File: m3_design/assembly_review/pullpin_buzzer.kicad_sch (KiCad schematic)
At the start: 10 parts, among them J123 BM02B-GHS-TBT(LF)(SN), Q123 AO3400A

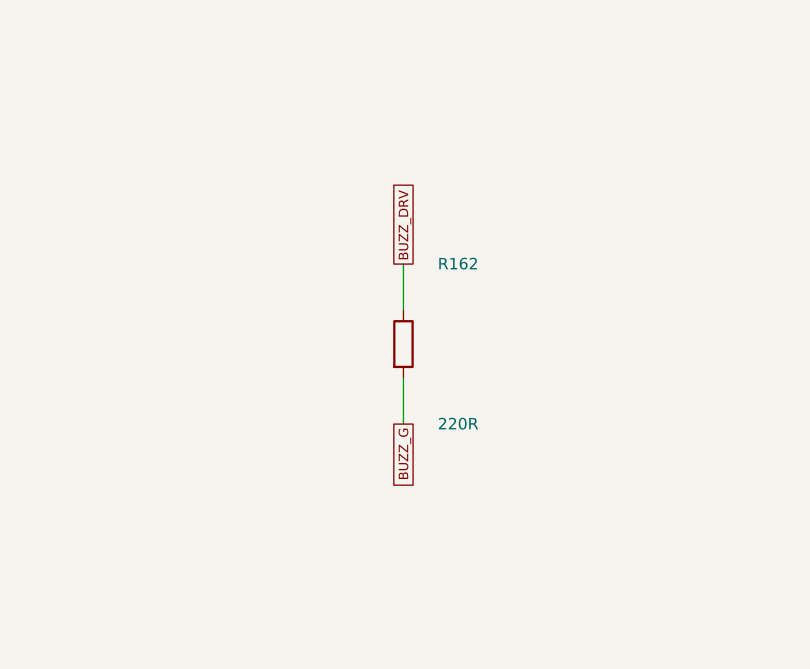
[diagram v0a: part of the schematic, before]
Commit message: R10 review round 3 and fix pass: ten-lens review of 883d2db5 (0 Critical, 7 Major, 49 Minor); In2 GND under the pyro column (S-8), U9 power path widened, In2 re-cut for the port control nets, GND vias at port-signal layer changes, crystal In2 GND restored, stitching, silkscreen >= 0.15 mm; gates: arcs, K-loader, S-8/S-9, wider critical set, needless hops, plate masses; R410 budget, R162 1k, F6 ride-through restated (OQ-5/OQ-6); board 579575bd..., check.sh 0
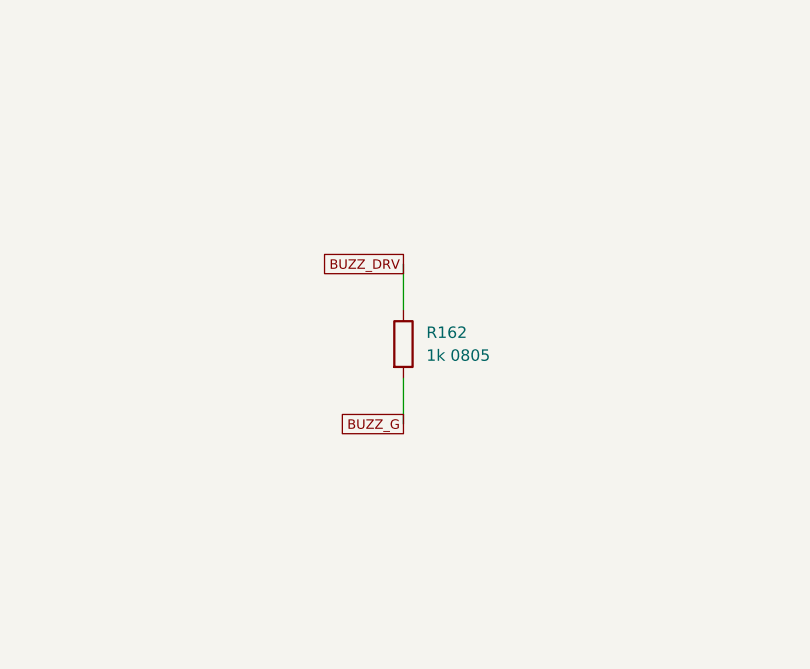
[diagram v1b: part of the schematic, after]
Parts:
- R162: value 220R -> 1k 0805; LCSC C17557 -> C17513; LCSC Part (none) -> C17513; Manufacturer Part 0805W8F2200T5E -> 0805W8F1001T5E
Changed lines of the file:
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@@
-	(symbol
-		(lib_id "M3:R")
-		(at 157.48 114.3 0)
-		(unit 1)
-		(in_bom yes)
-		(on_board yes)
-		(dnp no)
-		(property "Reference" "R162"
-			(at 161.29 105.41 0)
-			(effects
-				(font
-					(size 1.27 1.27))
-				(justify left)))
-		(property "Value" "220R"
-			(at 161.29 123.19 0)
-			(effects
-				(font
-					(size 1.27 1.27))
-				(justify left)))
-		(property "Footprint" "rocket:R0805"
-			(at 157.48 114.3 0)
-			(hide yes)
-			(effects
-				(font
-					(size 1.27 1.27))))
-		(property "Datasheet" ""
-			(at 157.48 114.3 0)
-			(hide yes)
-			(effects
-				(font
-					(size 1.27 1.27))))
-		(property "LCSC" "C17557"
-			(at 157.48 114.3 0)
-			(hide yes)
-			(effects
-				(font
-					(size 1.27 1.27))))
-		(property "Manufacturer" "UNI-ROYAL(Uniroyal Elec)"
-			(at 157.48 114.3 0)
-			(hide yes)
-			(effects
-				(font
-					(size 1.27 1.27))))
-		(property "Manufacturer Part" "0805W8F2200T5E"
-			(at 157.48 114.3 0)
-			(hide yes)
-			(effects
-				(font
-					(size 1.27 1.27))))
-		(instances
-			(project "m3"
-				(path "/6007a7db-6a58-5660-8beb-956dea045ff8/5ee931eb-d962-5c64-b0fd-46233c13323f"
-					(reference "R162")
-					(unit 1)))))
-	(wire
-		(pts
-			(xy 157.48 110.49)
-			(xy 157.48 105.41))
-		(stroke
-			(width 0)
-			(type default))
-)
-	(global_label "BUZZ_DRV"
-		(shape passive)
-		(at 157.48 105.41 90)
-		(effects
-			(font
-				(size 1.05 1.05))
-			(justify left))
-)
-	(wire
-		(pts
-			(xy 157.48 118.11)
-			(xy 157.48 123.19))
-		(stroke
-			(width 0)
-			(type default))
-)
-	(global_label "BUZZ_G"
-		(shape passive)
-		(at 157.48 123.19 270)
-		(effects
-			(font
-				(size 1.05 1.05))
-			(justify right))
-)
 	(symbol
 		(lib_id "M3:R")
@@
 		(effects
 			(font
+				(size 1.05 1.05))
+			(justify right))
+)
+	(symbol
+		(lib_id "M3:R")
+		(at 157.48 114.3 0)
+		(unit 1)
+		(in_bom yes)
+		(on_board yes)
+		(dnp no)
+		(property "Reference" "R162"
+			(at 160.02 113.03 0)
+			(effects
+				(font
+					(size 1.27 1.27))
+				(justify left)))
+		(property "Value" "1k 0805"
+			(at 160.02 115.57 0)
+			(effects
+				(font
+					(size 1.27 1.27))
+				(justify left)))
+		(property "Footprint" "rocket:R0805"
+			(at 157.48 114.3 0)
+			(hide yes)
+			(effects
+				(font
+					(size 1.27 1.27))
+				(justify left)))
+		(property "Datasheet" ""
+			(at 157.48 114.3 0)
+			(hide yes)
+			(effects
+				(font
+					(size 1.27 1.27))
+				(justify left)))
+		(property "LCSC" "C17513"
+			(at 157.48 114.3 0)
+			(hide yes)
+			(effects
+				(font
+					(size 1.27 1.27))
+				(justify left)))
+		(property "LCSC Part" "C17513"
+			(at 157.48 114.3 0)
+			(hide yes)
+			(effects
+				(font
+					(size 1.27 1.27))
+				(justify left)))
+		(property "Manufacturer" "UNI-ROYAL(Uniroyal Elec)"
+			(at 157.48 114.3 0)
+			(hide yes)
+			(effects
+				(font
+					(size 1.27 1.27))
+				(justify left)))
+		(property "Manufacturer Part" "0805W8F1001T5E"
+			(at 157.48 114.3 0)
+			(hide yes)
+			(effects
+				(font
+					(size 1.27 1.27))
+				(justify left)))
+		(instances
+			(project "m3"
+				(path "/6007a7db-6a58-5660-8beb-956dea045ff8/5ee931eb-d962-5c64-b0fd-46233c13323f"
+					(reference "R162")
+					(unit 1)))))
+	(wire
+		(pts
+			(xy 157.48 110.49)
+			(xy 157.48 105.41))
+		(stroke
+			(width 0)
+			(type default))
+)
+	(global_label "BUZZ_DRV"
+		(shape passive)
+		(at 157.48 105.41 0)
+		(effects
+			(font
+				(size 1.05 1.05))
+			(justify right))
+)
+	(wire
+		(pts
+			(xy 157.48 118.11)
+			(xy 157.48 123.19))
+		(stroke
+			(width 0)
+			(type default))
+)
+	(global_label "BUZZ_G"
+		(shape passive)
+		(at 157.48 123.19 0)
+		(effects
+			(font
